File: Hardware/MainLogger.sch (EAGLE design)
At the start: 210 parts, among them J3 GEMS_POWER_PLUGINPUT_RT, J4 U.FL, J5 SIM_CDNANO_SF72, Q1 DMG3404, Q2 MOSFET_PCH-DMP3036SFG, Q3 MOSFET_PCH-DMP3036SFG, Q4 DMG3404, Q5 NX2301P, Q6 NX2301P, U1 FXMAR2102UMLP, U10 SN74AUP3G34DCU, U11 TCK111G, U12 LTC4412S6, U13 TCR2LE31ESV, U14 LP59073.3VYKE, U15 MIC22602, U16 BQ25616, U17 TPS61282D, U18 MCP23018QFN, U19 MCP23018QFN, U2 VEML3328, U20 MAX-M8W, U21 MCP79412SOIC, U22 HALL_EFFECT_SI7201, U23 PCA9634QFN, U24 SN74LVC1G17DCK, U25 TPL5010DDC, U26 TPL5010DDC, U27 MB85RC, U28 FXMAR2102UMLP, U29 SIT1552, U3 MMC5633, U30 TCK111G, U31 FPF2195BUCX, U4 MXC6655, U5 PAC1934QFN, U6 PAC1934QFN, U7 SHT40, U8 SN74AUP1G08DCK, U9 FXMAR2102UMLP

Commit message: v1.5 Update
Updated schematic and layout, boards sent to fab
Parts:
- removed R43: 130k, bschulz_passives:R-EU_130KR0402
- removed R44: 30k, bschulz_passives:R-EU_30KR0402
- R38: value 150k -> 100k; device bschulz_passives:R-EU_150KR0402 -> bschulz_passives:R-EU_100KR0402
- R39: value 10k -> 100k; device bschulz_passives:R-EU_10KR0402 -> bschulz_passives:R-EU_100KR0402
- U18, U19: value MCP23018QFN -> PCAL9535AQFN; device bschulz:MCP23018QFN -> bschulz:PCAL9535AQFN
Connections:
- removed net N$35: R43.1, R44.2, U19.ADDR
- removed net N$38: R38.1, R39.2, U18.ADDR
- net !CE: now also U18.P1_3; no longer U18.GPB3
- net !RESET: no longer U18.!RESET, U19.!RESET
- net !TALON1_FAULT: now also U19.P0_2; no longer U19.GPA2
- net !TALON2_FAULT: now also U19.P0_6; no longer U19.GPA6
- net !TALON3_FAULT: now also U19.P1_2; no longer U19.GPB2
- net !TALON4_FAULT: now also U19.P1_6; no longer U19.GPB6
- net 3V3_AUX_EN: now also U18.P1_7; no longer U18.GPB7
- net 3V3_AUX_PG: now also U18.P0_0; no longer U18.GPA0
- net 3V3_CORE: now also R39.2, U19.A0; no longer R43.2
- net 3V3_SD_EN: now also U18.P1_4; no longer U18.GPB4
- net CHG_SOURCE: now also U18.P0_6; no longer U18.GPA6
- net CSA_EN: now also U18.P1_6; no longer U18.GPB6
- net GND: now also U18.A0, U18.A1, U18.A2, U19.A1, U19.A2; no longer R39.1, R44.1
- net GPS_INT: now also U18.P0_7; no longer U18.GPA7
- net I2C_EXT_EN: now also U18.P1_2; no longer U18.GPB2
- net LED_EN: now also U18.P1_5; no longer U18.GPB5
- net N$6: now also U18.P0_4; no longer U18.GPA4
- net N$8: now also U18.P0_5; no longer U18.GPA5
- net N$9: now also U18.P0_3; no longer U18.GPA3
- net OB_INT: now also R39.1, U18.!INT; no longer U18.INTA
- net SD_CD: now also U18.P1_0; no longer U18.GPB0
- net SENSOR_INT: now also U18.P0_2; no longer U18.GPA2
- net SIM_CD: now also U18.P1_1; no longer U18.GPB1
- net TALON1_EN: now also U19.P0_3; no longer U19.GPA3
- net TALON1_I2C_EN: now also U19.P0_1; no longer U19.GPA1
- net TALON1_SEL: now also U19.P0_0; no longer U19.GPA0
- net TALON2_EN: now also U19.P0_7; no longer U19.GPA7
- net TALON2_I2C_EN: now also U19.P0_5; no longer U19.GPA5
- net TALON2_SEL: now also U19.P0_4; no longer U19.GPA4
- net TALON3_EN: now also U19.P1_3; no longer U19.GPB3
- net TALON3_I2C_EN: now also U19.P1_1; no longer U19.GPB1
- net TALON3_SEL: now also U19.P1_0; no longer U19.GPB0
- net TALON4_EN: now also U19.P1_7; no longer U19.GPB7
- net TALON4_I2C_EN: now also U19.P1_5; no longer U19.GPB5
- net TALON4_SEL: now also U19.P1_4; no longer U19.GPB4
- net TALON_INT: now also R38.1, U19.!INT; no longer U19.INTA
- net VBULK_PG: now also U18.P0_1; no longer U18.GPA1
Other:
- moved on the sheet: C38, C39, R38, R39

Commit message: v1.6 Update
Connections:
- net BAT_CHG: no longer C49.1, D4.A2, R54.1, R55.1, U24.VCC, U25.VDD
- net SYSCORE: now also C49.1, D4.A2, R54.1, R55.1, U24.VCC, U25.VDD
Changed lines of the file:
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@@
 <setting verticaltext="up"/>
 </settings>
-<grid distance="0.1" unitdist="inch" unit="mm" style="lines" multiple="1" display="no" altdistance="0.01" altunitdist="inch" altunit="inch"/>
+<grid distance="0.1" unitdist="inch" unit="inch" style="lines" multiple="1" display="no" altdistance="0.01" altunitdist="inch" altunit="inch"/>
 <layers>
 <layer number="1" name="Top" color="4" fill="1" visible="no" active="no"/>
@@
 <label x="231.14" y="129.54" size="1.016" layer="95" rot="R180" xref="yes"/>
 </segment>
-<segment>
-<pinref part="D4" gate="G$1" pin="A2"/>
-<wire x1="124.46" y1="73.66" x2="124.46" y2="66.04" width="0.1524" layer="91"/>
-<wire x1="124.46" y1="66.04" x2="119.38" y2="66.04" width="0.1524" layer="91"/>
-<label x="119.38" y="66.04" size="1.016" layer="95" rot="R180" xref="yes"/>
-</segment>
 </net>
 <net name="REGN" class="0">
@@
 <label x="251.46" y="170.18" size="0.8128" layer="95" xref="yes"/>
 </segment>
+<segment>
+<pinref part="D4" gate="G$1" pin="A2"/>
+<wire x1="124.46" y1="73.66" x2="124.46" y2="66.04" width="0.1524" layer="91"/>
+<wire x1="124.46" y1="66.04" x2="119.38" y2="66.04" width="0.1524" layer="91"/>
+<label x="119.38" y="66.04" size="1.016" layer="95" rot="R180" xref="yes"/>
+</segment>
 </net>
 <net name="BTST" class="0">
@@
 </segment>
 </net>
-<net name="BAT_CHG" class="0">
-<segment>
-<pinref part="U25" gate="G$1" pin="VDD"/>
-<wire x1="241.3" y1="134.62" x2="238.76" y2="134.62" width="0.1524" layer="91"/>
-<label x="238.76" y="134.62" size="1.016" layer="95" rot="R180" xref="yes"/>
-</segment>
-<segment>
-<pinref part="C49" gate="G$1" pin="1"/>
-<wire x1="215.9" y1="132.08" x2="215.9" y2="134.62" width="0.1524" layer="91"/>
-<wire x1="215.9" y1="134.62" x2="213.36" y2="134.62" width="0.1524" layer="91"/>
-<label x="213.36" y="134.62" size="1.016" layer="95" rot="R180" xref="yes"/>
-</segment>
-<segment>
-<pinref part="R55" gate="G$1" pin="1"/>
-<wire x1="228.6" y1="172.72" x2="228.6" y2="175.26" width="0.1524" layer="91"/>
-<wire x1="228.6" y1="175.26" x2="231.14" y2="175.26" width="0.1524" layer="91"/>
-<label x="231.14" y="175.26" size="0.8128" layer="95" xref="yes"/>
-</segment>
-<segment>
-<pinref part="R54" gate="G$1" pin="1"/>
-<wire x1="215.9" y1="193.04" x2="218.44" y2="193.04" width="0.1524" layer="91"/>
-<label x="218.44" y="193.04" size="1.016" layer="95" xref="yes"/>
-</segment>
-<segment>
-<pinref part="U24" gate="G$1" pin="VCC"/>
-<wire x1="259.08" y1="157.48" x2="261.62" y2="157.48" width="0.1524" layer="91"/>
-<label x="261.62" y="157.48" size="1.016" layer="95" xref="yes"/>
-</segment>
-</net>
 <net name="N$30" class="0">
 <segment>
@@
 </segment>
 </net>
+<net name="SYSCORE" class="0">
+<segment>
+<pinref part="U25" gate="G$1" pin="VDD"/>
+<wire x1="241.3" y1="134.62" x2="238.76" y2="134.62" width="0.1524" layer="91"/>
+<label x="238.76" y="134.62" size="1.016" layer="95" rot="R180" xref="yes"/>
+</segment>
+<segment>
+<pinref part="U24" gate="G$1" pin="VCC"/>
+<wire x1="259.08" y1="157.48" x2="261.62" y2="157.48" width="0.1524" layer="91"/>
+<label x="261.62" y="157.48" size="1.016" layer="95" xref="yes"/>
+</segment>
+<segment>
+<pinref part="R55" gate="G$1" pin="1"/>
+<wire x1="228.6" y1="172.72" x2="228.6" y2="175.26" width="0.1524" layer="91"/>
+<wire x1="228.6" y1="175.26" x2="231.14" y2="175.26" width="0.1524" layer="91"/>
+<label x="231.14" y="175.26" size="0.8128" layer="95" xref="yes"/>
+</segment>
+<segment>
+<pinref part="R54" gate="G$1" pin="1"/>
+<wire x1="215.9" y1="193.04" x2="218.44" y2="193.04" width="0.1524" layer="91"/>
+<label x="218.44" y="193.04" size="1.016" layer="95" xref="yes"/>
+</segment>
+<segment>
+<pinref part="C49" gate="G$1" pin="1"/>
+<wire x1="215.9" y1="132.08" x2="215.9" y2="134.62" width="0.1524" layer="91"/>
+<wire x1="215.9" y1="134.62" x2="213.36" y2="134.62" width="0.1524" layer="91"/>
+<label x="213.36" y="134.62" size="1.016" layer="95" rot="R180" xref="yes"/>
+</segment>
+</net>

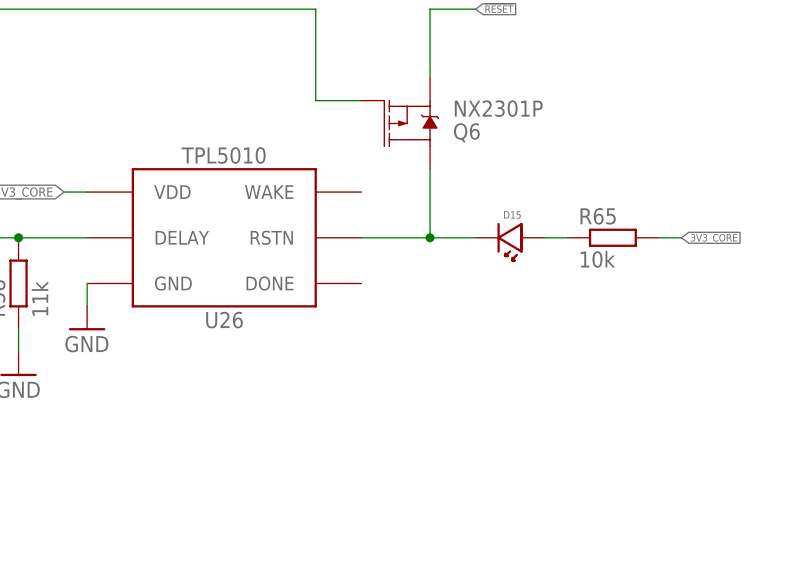
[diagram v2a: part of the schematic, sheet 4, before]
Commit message: Added fix for WDT
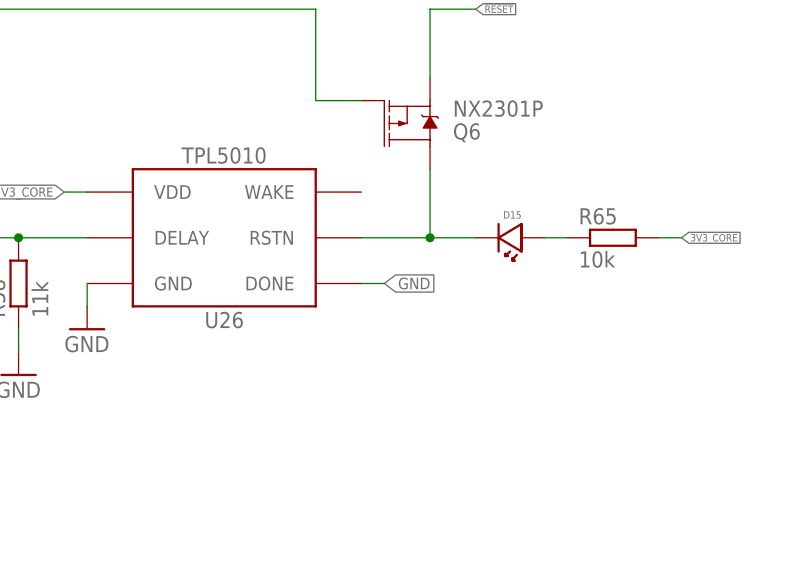
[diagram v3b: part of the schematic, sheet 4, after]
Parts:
- TP1, TP2, TP5, TP6, TP7, TP8, TP9: value TESTPOINTRCU -> TESTPOINT_DNP_RCU; device bschulz:TESTPOINTRCU -> bschulz:TESTPOINT_DNP_RCU
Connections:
- net GND: now also U26.DONE
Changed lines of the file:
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@@
 <part name="U8" library="bschulz" deviceset="SN74AUP1G08" device="DCK"/>
 <part name="GND53" library="supply1" library_urn="urn:adsk.eagle:library:371" deviceset="GND" device=""/>
-<part name="TP1" library="bschulz" deviceset="TESTPOINT" device="RCU"/>
-<part name="TP2" library="bschulz" deviceset="TESTPOINT" device="RCU"/>
-<part name="TP5" library="bschulz" deviceset="TESTPOINT" device="RCU"/>
-<part name="TP6" library="bschulz" deviceset="TESTPOINT" device="RCU"/>
-<part name="TP7" library="bschulz" deviceset="TESTPOINT" device="RCU"/>
-<part name="TP8" library="bschulz" deviceset="TESTPOINT" device="RCU"/>
-<part name="TP9" library="bschulz" deviceset="TESTPOINT" device="RCU"/>
+<part name="TP1" library="bschulz" deviceset="TESTPOINT" device="RCU" technology="_DNP_" value="TESTPOINT_DNP_RCU"/>
+<part name="TP2" library="bschulz" deviceset="TESTPOINT" device="RCU" technology="_DNP_" value="TESTPOINT_DNP_RCU"/>
+<part name="TP5" library="bschulz" deviceset="TESTPOINT" device="RCU" technology="_DNP_" value="TESTPOINT_DNP_RCU"/>
+<part name="TP6" library="bschulz" deviceset="TESTPOINT" device="RCU" technology="_DNP_" value="TESTPOINT_DNP_RCU"/>
+<part name="TP7" library="bschulz" deviceset="TESTPOINT" device="RCU" technology="_DNP_" value="TESTPOINT_DNP_RCU"/>
+<part name="TP8" library="bschulz" deviceset="TESTPOINT" device="RCU" technology="_DNP_" value="TESTPOINT_DNP_RCU"/>
+<part name="TP9" library="bschulz" deviceset="TESTPOINT" device="RCU" technology="_DNP_" value="TESTPOINT_DNP_RCU"/>
 <part name="R9" library="bschulz_passives" deviceset="R-EU_" device="R0402" technology="27" value="27R"/>
 <part name="R10" library="bschulz_passives" deviceset="R-EU_" device="R0402" technology="27" value="27R"/>
@@
 <junction x="48.26" y="312.42"/>
 </segment>
+<segment>
+<pinref part="U26" gate="G$1" pin="DONE"/>
+<wire x1="274.32" y1="55.88" x2="276.86" y2="55.88" width="0.1524" layer="91"/>
+<label x="276.86" y="55.88" size="1.27" layer="95" xref="yes"/>
+</segment>
 </net>

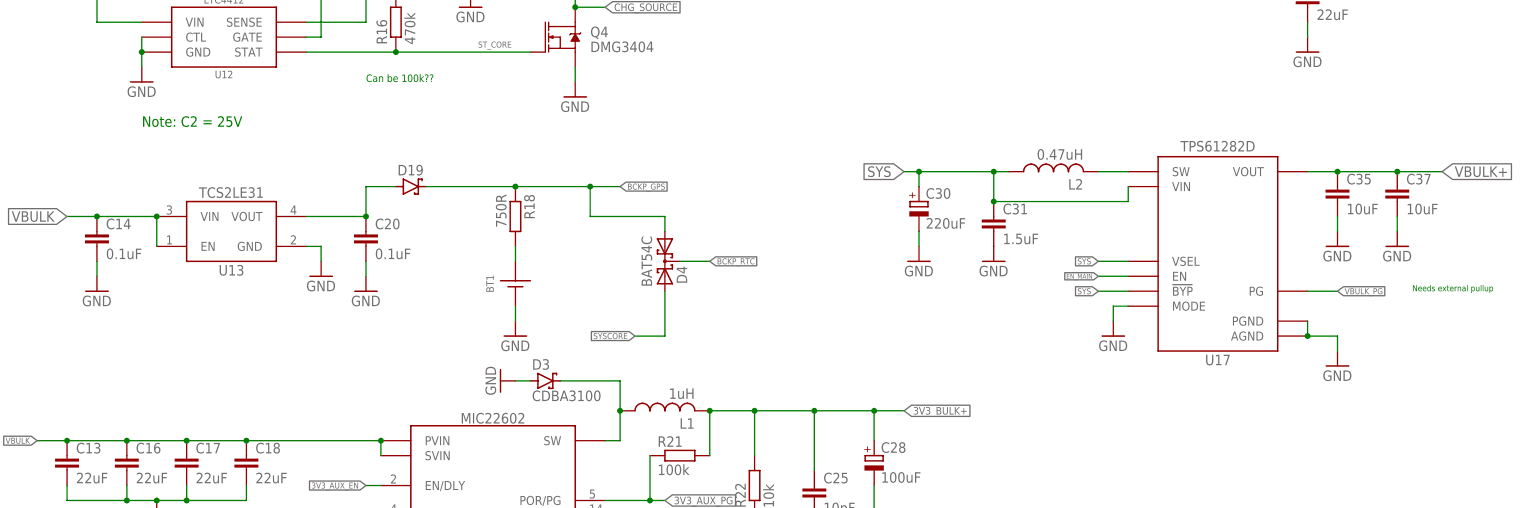
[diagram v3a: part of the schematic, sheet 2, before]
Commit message: v1.8 Updates
- Changed accel (#1)
- Fixed backup regulator issue (#16)
- Fixed TCXO overvoltage issue (#19)
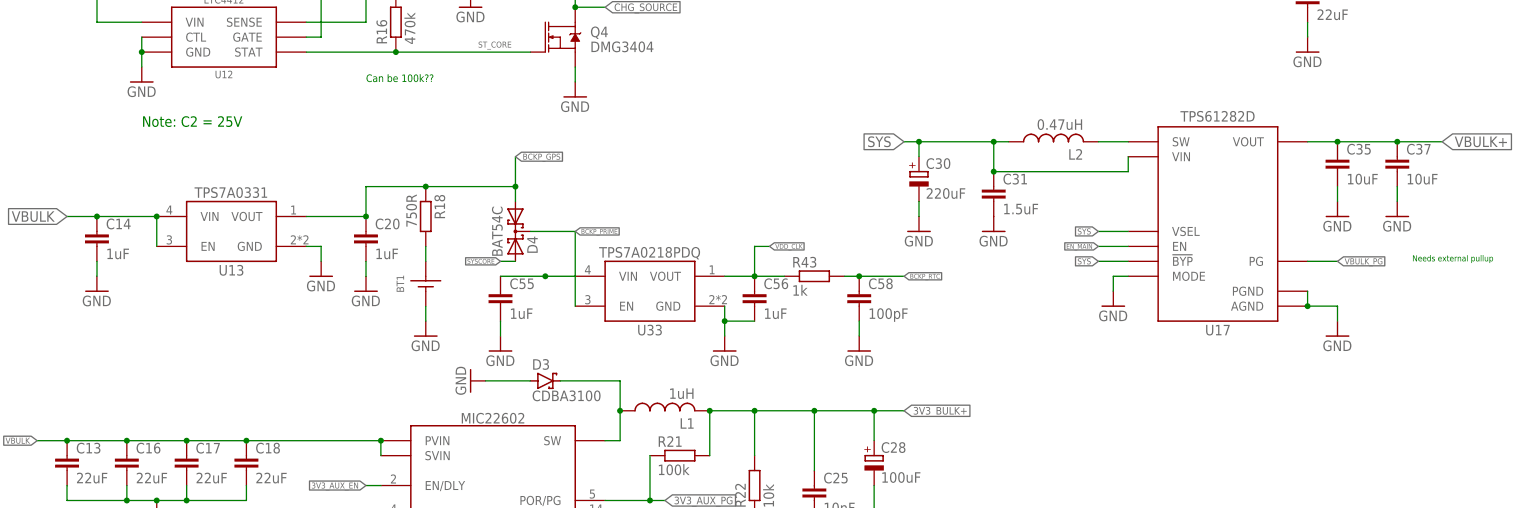
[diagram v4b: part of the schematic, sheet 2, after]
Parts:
- removed D19: (no value), bschulz:DIODE_SCHOTTKYSOD-323
- added C55, C56: 1uF, bschulz_passives:C-EU1UFC0603
- added C57: 0.1uF, bschulz_passives:C-EU0.1UFC0402
- added C58: 100pF, bschulz_passives:C-EU100PFC0402
- added R43: 1k, bschulz_passives:R-EU_1KR0402
- added U33: TPS7A0218PDQ, bschulz:TPS7A0218PDQ
- C14, C20: value 0.1uF -> 1uF; device bschulz_passives:C-EU0.1UFC0402 -> bschulz_passives:C-EU1UFC0603
- C3: value 2.2uF -> 0.1uF; device bschulz_passives:C-EU2.2UFC0603 -> bschulz_passives:C-EU0.1UFC0402
- D11, D14, D17, D7: value LEDAMBER0603 -> LEDYELLOW0603; device bschulz:LEDAMBER0603 -> bschulz:LEDYELLOW0603
- U13: value TCR2LE31ESV -> TPS7A0331PDQ; device bschulz:TCR2LE31ESV -> bschulz:TPS7A0331PDQ
- U4: value MXC6655 -> BMA456; device bschulz:MXC6655 -> bschulz:BMA456
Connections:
- net N$4 renamed CLK_OSC
- removed net N$3: C20.1, D19.A, U13.VOUT
- new net BCKP_PRIME: C55.1, D4.C, U33.EN, U33.VIN
- new net VDD_CLK: C56.1, R43.1, U29.VCC, U33.VOUT
- net 3V3_AUX_EN: now also U32.A; no longer U32G1.A
- net 3V3_CORE: now also C57.1, U32.VCC; no longer U32G2.P$V+
- net BCKP_GPS: now also C20.1, U13.VOUT; no longer D19.C
- net BCKP_RTC: now also C58.1, R43.2; no longer D4.C, U29.VCC
- net GND: now also C55.2, C56.2, C57.2, C58.2, U32.GND, U33.GND; no longer U32G2.P$V-
- net N$28: now also U32.Y; no longer U32G1.Y
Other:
- note added: "ADR: 0x18"
- note removed: "ADR: 0x15"
- note removed: "Should this be 3V3 Core or 3V3 AUX??"
- moved on the sheet: BT1, C3, C30, C31, C35, C37, D4, L2, R18, U13, U17

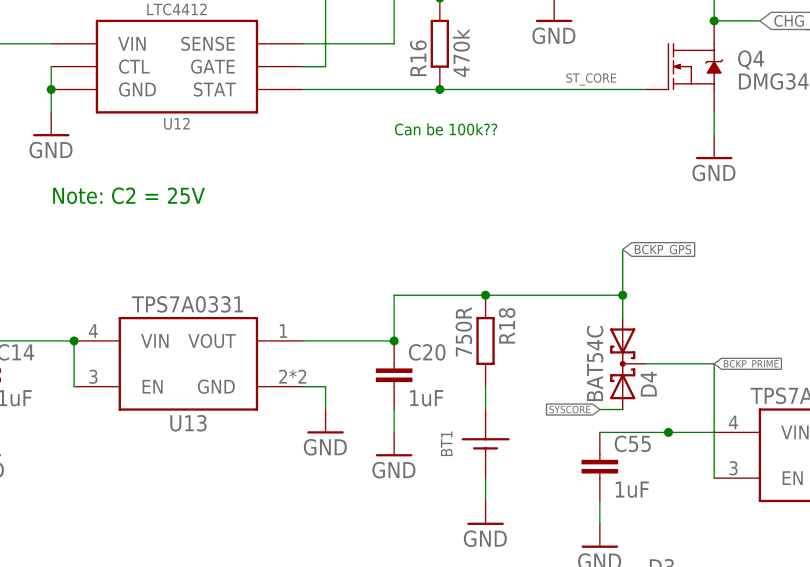
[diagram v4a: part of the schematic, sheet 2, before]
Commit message: v1.9 updates
Added series diode in gps/rtc bat charger to prevent reverse current
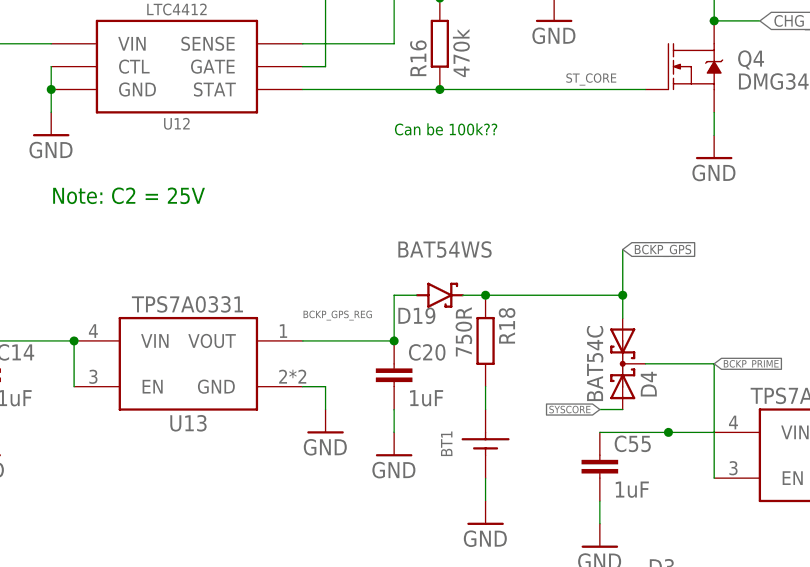
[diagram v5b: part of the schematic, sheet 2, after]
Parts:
- added D19: BAT54WS, bschulz:DIODE_SCHOTTKYSOD-323
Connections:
- new net BCKP_GPS_REG: C20.1, D19.A, U13.VOUT
- net BCKP_GPS: now also D19.C; no longer C20.1, U13.VOUT
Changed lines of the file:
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@@
 <part name="R43" library="bschulz_passives" deviceset="R-EU_" device="R0402" technology="1K" value="1k"/>
 <part name="GND92" library="supply1" library_urn="urn:adsk.eagle:library:371" deviceset="GND" device=""/>
+<part name="D19" library="bschulz" deviceset="DIODE_SCHOTTKY" device="SOD-323" value="BAT54WS">
+<attribute name="DIGIKEY" value="BAT54WS-TPCT-ND"/>
+<attribute name="MF" value="Micro Commercial"/>
+<attribute name="MPN" value="BAT54WS-TP"/>
+</part>
 </parts>
 <sheets>
@@
 <attribute name="VALUE" x="154.94" y="60.96" size="1.778" layer="96"/>
 </instance>
+<instance part="D19" gate="G$1" x="78.74" y="91.44" smashed="yes">
+<attribute name="NAME" x="73.914" y="88.265" size="1.778" layer="95"/>
+<attribute name="VALUE" x="73.914" y="95.631" size="1.778" layer="96"/>
+</instance>
 </instances>
 <busses>
@@
 <pinref part="R18" gate="G$1" pin="1"/>
 <wire x1="83.82" y1="91.44" x2="99.06" y2="91.44" width="0.1524" layer="91"/>
-<junction x="83.82" y="91.44"/>
 <wire x1="99.06" y1="91.44" x2="99.06" y2="96.52" width="0.1524" layer="91"/>
 <junction x="99.06" y="91.44"/>
 <pinref part="D4" gate="G$1" pin="A1"/>
 <wire x1="99.06" y1="91.44" x2="99.06" y2="88.9" width="0.1524" layer="91"/>
-<pinref part="U13" gate="G$1" pin="VOUT"/>
-<pinref part="C20" gate="G$1" pin="1"/>
-<wire x1="63.5" y1="86.36" x2="73.66" y2="86.36" width="0.1524" layer="91"/>
-<wire x1="73.66" y1="86.36" x2="73.66" y2="91.44" width="0.1524" layer="91"/>
-<junction x="73.66" y="86.36"/>
-<wire x1="73.66" y1="91.44" x2="83.82" y2="91.44" width="0.1524" layer="91"/>
+<pinref part="D19" gate="G$1" pin="C"/>
+<wire x1="81.28" y1="91.44" x2="83.82" y2="91.44" width="0.1524" layer="91"/>
+<junction x="83.82" y="91.44"/>
 </segment>
 </net>
@@
 </segment>
 </net>
+<net name="BCKP_GPS_REG" class="0">
+<segment>
+<pinref part="C20" gate="G$1" pin="1"/>
+<pinref part="U13" gate="G$1" pin="VOUT"/>
+<wire x1="63.5" y1="86.36" x2="73.66" y2="86.36" width="0.1524" layer="91"/>
+<wire x1="73.66" y1="86.36" x2="73.66" y2="91.44" width="0.1524" layer="91"/>
+<junction x="73.66" y="86.36"/>
+<label x="63.5" y="88.9" size="0.8128" layer="95"/>
+<pinref part="D19" gate="G$1" pin="A"/>
+<wire x1="76.2" y1="91.44" x2="73.66" y2="91.44" width="0.1524" layer="91"/>
+</segment>
+</net>
